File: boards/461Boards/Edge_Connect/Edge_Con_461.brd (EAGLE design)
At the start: 56.8 x 57.1 mm, 8 parts, among them IC1 TINY26P

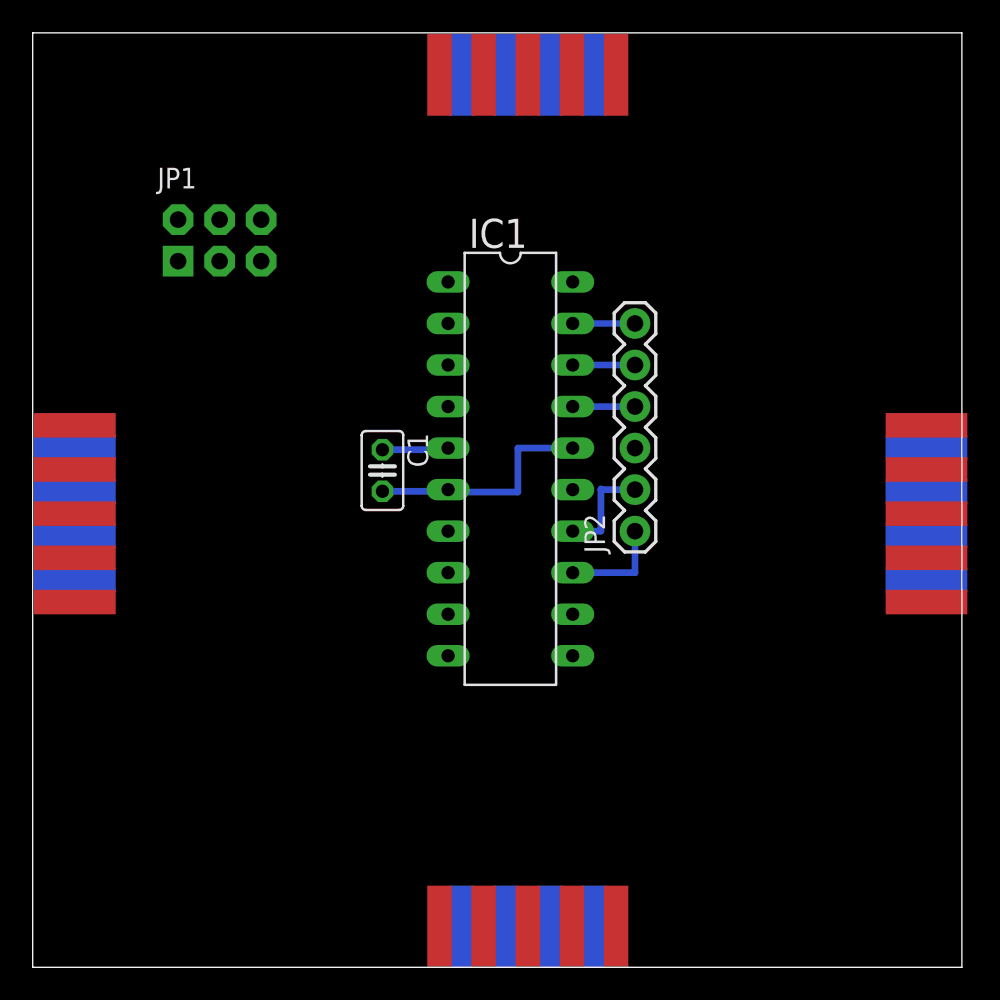
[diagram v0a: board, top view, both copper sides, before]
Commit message: Layout in progress, one footprint needs to be added to 461_Edge Connect prior to cut.
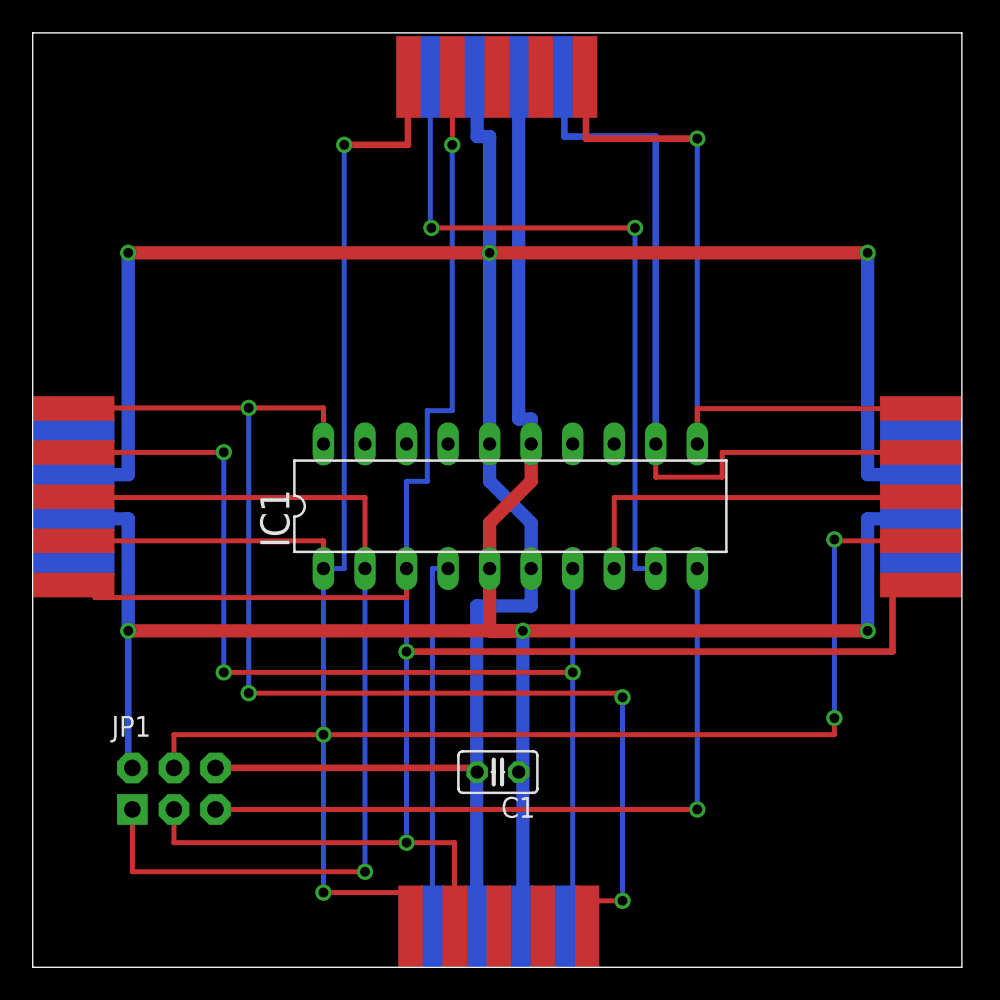
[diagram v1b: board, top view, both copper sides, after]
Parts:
- removed JP2: (no value), SparkFun-Connectors:1X06
- moved JP1 33.6 mm to (8.64, 10.9)
- moved C1 19.7 mm to (28.4, 11.9), turned to 180 degrees
- moved RIGHT 14.4 mm to (51.8, 34.9), turned to 270 degrees
- moved LEFT 14.3 mm to (0.00, 34.9), turned to 270 degrees
- moved IC1 2.29 mm to (29.2, 28.2), turned to 0 degrees
- moved UP 1.91 mm to (22.2, 51.9)
- moved DOWN 1.78 mm to (22.4, 0.00)
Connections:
- removed net 16: JP2.3
- net 13: no longer JP2.1
- net 14: no longer JP2.2
- net 17: no longer JP2.4
- net 18: no longer JP2.5
- net 19: no longer JP2.6
- net CLK_IN: now also DOWN.P$9, LEFT.P$2; no longer DOWN.P$1, LEFT.P$1
- net CLK_OUT: now also RIGHT.P$2, UP.P$9; no longer RIGHT.P$1, UP.P$1
- net DOWN: now also DOWN.P$6; no longer DOWN.P$2
- net GND: no longer DOWN.P$8, LEFT.P$8, RIGHT.P$8, UP.P$8
- net LEFT: now also LEFT.P$3; no longer LEFT.P$2
- net MDO: now also RIGHT.P$1; no longer RIGHT.P$5
- net RIGHT: now also RIGHT.P$3; no longer RIGHT.P$2
- net SCL: now also DOWN.P$2, LEFT.P$5, RIGHT.P$5, UP.P$2; no longer DOWN.P$4, LEFT.P$4, RIGHT.P$4, UP.P$4
- net SDA: now also DOWN.P$1, LEFT.P$4, RIGHT.P$4, UP.P$1; no longer DOWN.P$3, LEFT.P$3, RIGHT.P$3, UP.P$3
- net SDI: now also LEFT.P$1; no longer LEFT.P$5
- net UP: now also UP.P$6; no longer UP.P$2
- net VCC: now also DOWN.P$8, LEFT.P$8, RIGHT.P$8, UP.P$8; no longer DOWN.P$6, DOWN.P$9, LEFT.P$6, LEFT.P$9, RIGHT.P$6, RIGHT.P$9, UP.P$6, UP.P$9
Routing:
- net SDA: track 0.00 -> 139.1 mm, vias 0 -> 5
- net GND: track 14.5 -> 152.5 mm, vias 0 -> 3
- net SCL: track 0.00 -> 132.4 mm, vias 0 -> 3
- net VCC: track 5.13 -> 130.3 mm, vias 0 -> 3
- net SDI: track 0.00 -> 71.3 mm, vias 0 -> 4
- net CLK_IN: track 0.00 -> 64.2 mm, vias 0 -> 3
- net LEFT: track 0.00 -> 57.3 mm, vias 0 -> 1
- net CLK_OUT: track 0.00 -> 50.1 mm
- net MDO: track 0.00 -> 49.3 mm, vias 0 -> 1
- net UP: track 0.00 -> 44.7 mm, vias 0 -> 2
- net N$1: track 0.00 -> 44.2 mm, vias 0 -> 1
- net RIGHT: track 0.00 -> 24.5 mm
- net DOWN: track 0.00 -> 22.0 mm
- net 14: track 6.40 -> 0.00 mm
- net 13: track 6.35 -> 0.00 mm
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
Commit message: Edge Connect Layout Complete V1.0, 3 Jumper Function Select, 2 LED spaces available, Push Button Reset.
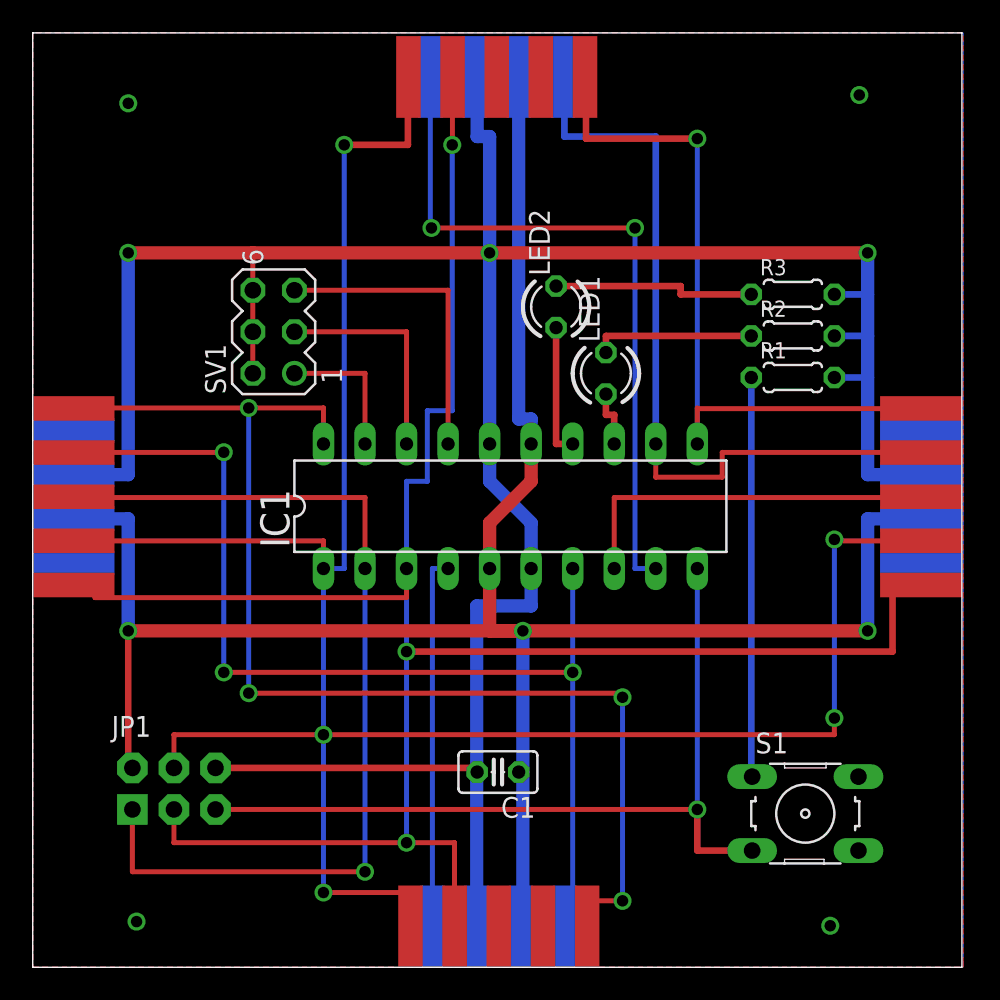
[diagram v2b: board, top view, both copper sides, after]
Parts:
- added LED1, LED2: (no value), led:LED3MM
- added R1, R2, R3: (no value), rcl:0204/5
- added S1: (no value), switch-omron:B3F-10XX
- added SV1: (no value), con-lstb:MA03-2
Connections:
- new net N$2: R1.1, S1.1
- new net N$3: LED1.K, R2.1
- new net N$4: LED2.K, R3.1
- net 13: now also LED1.A
- net 14: now also LED2.A
- net 17: now also SV1.5
- net 18: now also SV1.3
- net 19: now also SV1.1
- net GND: now also R1.2, R2.2, R3.2, SV1.2, SV1.4, SV1.6
- net N$1: now also S1.3
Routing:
- net N$2: track 0.00 -> 24.5 mm
- net 17: track 0.00 -> 18.8 mm
- net 18: track 0.00 -> 13.7 mm
- net GND: track 152.5 -> 165.9 mm, vias 3 -> 7
- net N$4: track 0.00 -> 12.4 mm
- net N$3: track 0.00 -> 9.91 mm
- net 19: track 0.00 -> 8.64 mm
- net 14: track 0.00 -> 8.13 mm
- net N$1: track 44.2 -> 50.1 mm
- net 13: track 0.00 -> 3.56 mm
- added copper zone on layer 1, net GND
- added copper zone on layer 16, net GND

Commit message: Moved Pull-up resistor to be pull up resistor on Edge Connect 461 board.
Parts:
- moved R1 9.52 mm to (45.0, 26.7), turned to 270 degrees
- moved S1 2.55 mm to (49.8, 9.65)
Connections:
- removed net N$2: R1.1, S1.1
- net GND: now also S1.1; no longer R1.2
- net N$1: now also R1.2
- net VCC: now also R1.1
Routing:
- net N$2: track 24.5 -> 0.00 mm
- net GND: track 165.9 -> 183.3 mm
- net VCC: track 130.6 -> 138.5 mm
- net N$1: track 50.1 -> 57.3 mm
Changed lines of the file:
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@@
 <attribute name="OC_FARNELL" value="unknown" x="14.732" y="38.862" size="1.778" layer="27" rot="R90" display="off"/>
 </element>
-<element name="S1" library="switch-omron" package="B3F-10XX" value="" x="47.244" y="9.398">
-<attribute name="OC_NEWARK" value="36M3542" x="47.244" y="9.398" size="1.778" layer="27" display="off"/>
-<attribute name="MPN" value="B3F-1000" x="47.244" y="9.398" size="1.778" layer="27" display="off"/>
-<attribute name="MF" value="" x="47.244" y="9.398" size="1.778" layer="27" display="off"/>
-<attribute name="OC_FARNELL" value="176432" x="47.244" y="9.398" size="1.778" layer="27" display="off"/>
+<element name="S1" library="switch-omron" package="B3F-10XX" value="" x="49.784" y="9.652">
+<attribute name="OC_NEWARK" value="36M3542" x="49.784" y="9.652" size="1.778" layer="27" display="off"/>
+<attribute name="MPN" value="B3F-1000" x="49.784" y="9.652" size="1.778" layer="27" display="off"/>
+<attribute name="MF" value="" x="49.784" y="9.652" size="1.778" layer="27" display="off"/>
+<attribute name="OC_FARNELL" value="176432" x="49.784" y="9.652" size="1.778" layer="27" display="off"/>
 </element>
-<element name="R1" library="rcl" package="0204/5" value="" x="46.482" y="36.068"/>
+<element name="R1" library="rcl" package="0204/5" value="" x="44.958" y="26.67" rot="R270"/>
 <element name="R2" library="rcl" package="0204/5" value="" x="46.482" y="38.608"/>
 <element name="R3" library="rcl" package="0204/5" value="" x="46.482" y="41.148"/>
@@
 <wire x1="5.842" y1="20.574" x2="5.842" y2="12.192" width="0.4064" layer="1"/>
 <wire x1="5.842" y1="12.192" x2="6.096" y2="12.192" width="0.4064" layer="1"/>
+<contactref element="R1" pad="1"/>
+<wire x1="44.958" y1="29.21" x2="47.498" y2="29.21" width="0.4064" layer="16"/>
+<wire x1="47.498" y1="29.21" x2="47.498" y2="27.425" width="0.4064" layer="16"/>
+<wire x1="47.498" y1="27.425" x2="51.054" y2="27.425" width="0.4064" layer="16"/>
 </signal>
 <signal name="GND">
@@
 <wire x1="13.462" y1="43.688" x2="27.94" y2="43.688" width="0.8128" layer="1"/>
 <wire x1="55.126" y1="30.125" x2="51.054" y2="30.125" width="0.8128" layer="16"/>
-<wire x1="51.054" y1="30.125" x2="51.054" y2="36.068" width="0.8128" layer="16"/>
+<wire x1="51.054" y1="30.125" x2="51.054" y2="38.608" width="0.8128" layer="16"/>
 <via x="51.054" y="43.688" extent="1-16" drill="0.7"/>
-<wire x1="51.054" y1="36.068" x2="51.054" y2="38.608" width="0.8128" layer="16"/>
 <wire x1="51.054" y1="38.608" x2="51.054" y2="41.148" width="0.8128" layer="16"/>
 <wire x1="51.054" y1="41.148" x2="51.054" y2="43.688" width="0.8128" layer="16"/>
@@
 <wire x1="13.462" y1="38.862" x2="13.462" y2="41.402" width="0.3048" layer="1"/>
 <wire x1="13.462" y1="41.402" x2="13.462" y2="43.688" width="0.3048" layer="1"/>
-<contactref element="R1" pad="2"/>
 <contactref element="R2" pad="2"/>
 <contactref element="R3" pad="2"/>
 <wire x1="49.022" y1="41.148" x2="51.054" y2="41.148" width="0.4064" layer="16"/>
 <wire x1="49.022" y1="38.608" x2="51.054" y2="38.608" width="0.4064" layer="16"/>
-<wire x1="49.022" y1="36.068" x2="51.054" y2="36.068" width="0.4064" layer="16"/>
 <polygon width="0.4064" layer="1" isolate="0.4064">
 <vertex x="0" y="0"/>
@@
 <via x="48.768" y="2.54" extent="1-16" drill="0.7"/>
 <via x="6.35" y="2.794" extent="1-16" drill="0.7"/>
+<contactref element="S1" pad="1"/>
+<wire x1="27.178" y1="11.938" x2="46.5074" y2="11.938" width="0.4064" layer="1"/>
+<wire x1="46.5074" y1="11.938" x2="46.5328" y2="11.9126" width="0.4064" layer="1"/>
 </signal>
 <signal name="13">
@@
 <via x="40.64" y="9.652" extent="1-16" drill="0.7"/>
 <wire x1="40.64" y1="9.652" x2="40.64" y2="24.384" width="0.3048" layer="16"/>
+<wire x1="40.64" y1="9.652" x2="40.64" y2="7.1374" width="0.4064" layer="1"/>
+<contactref element="R1" pad="2"/>
 <contactref element="S1" pad="3"/>
-<wire x1="40.64" y1="9.652" x2="40.64" y2="7.1374" width="0.4064" layer="1"/>
-<wire x1="40.64" y1="7.1374" x2="43.9928" y2="7.1374" width="0.4064" layer="1"/>
-</signal>
-<signal name="N$2">
-<contactref element="S1" pad="1"/>
-<contactref element="R1" pad="1"/>
-<wire x1="43.942" y1="36.068" x2="43.942" y2="11.6586" width="0.4064" layer="16"/>
-<wire x1="43.942" y1="11.6586" x2="43.9928" y2="11.6586" width="0.4064" layer="16"/>
+<wire x1="40.64" y1="7.1374" x2="46.2788" y2="7.1374" width="0.4064" layer="1"/>
+<wire x1="46.2788" y1="7.1374" x2="46.5328" y2="7.3914" width="0.4064" layer="1"/>
+<wire x1="40.64" y1="24.384" x2="40.64" y2="24.13" width="0.4064" layer="16"/>
+<wire x1="40.64" y1="24.13" x2="44.958" y2="24.13" width="0.4064" layer="16"/>
 </signal>
 <signal name="N$3">

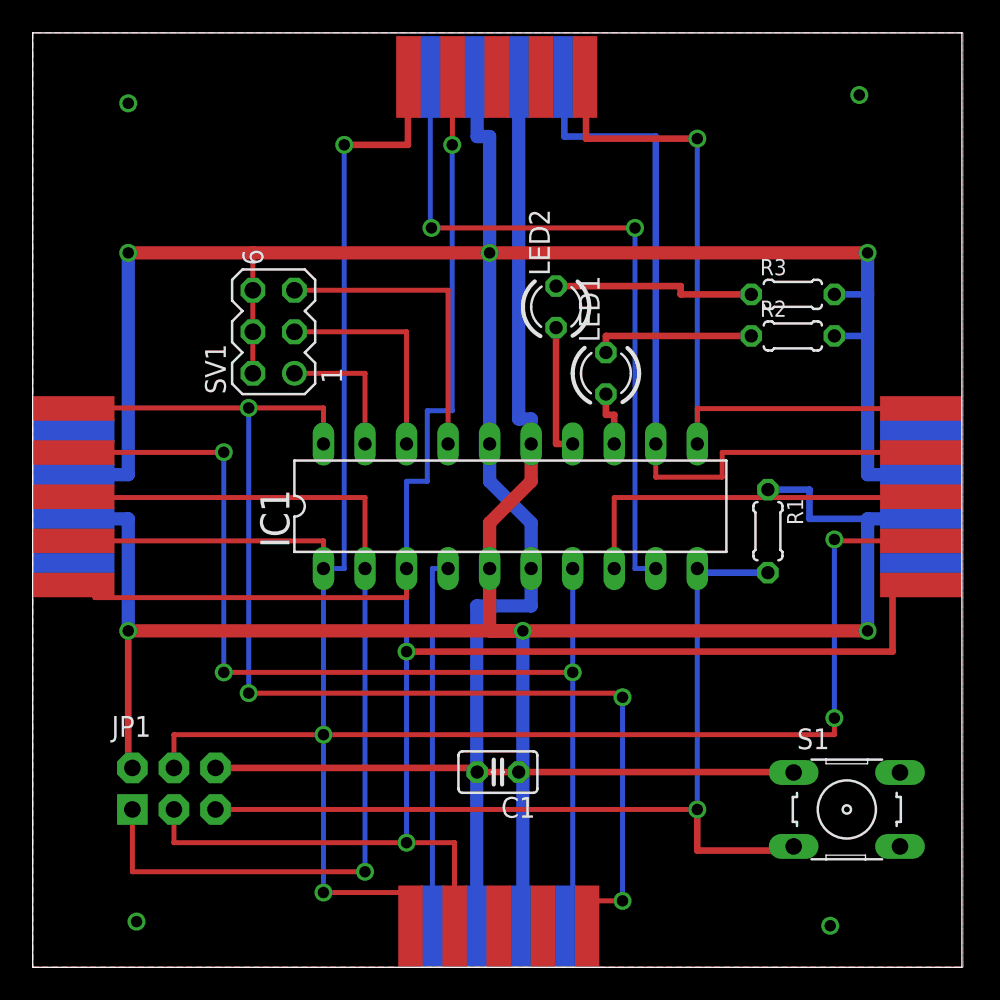
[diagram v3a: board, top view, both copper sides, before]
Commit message: v1.1 Edge Connect Prototype Board Changes: Widened power and ground traces. Added power LED indicator. Increased all via diameters for easier plating.
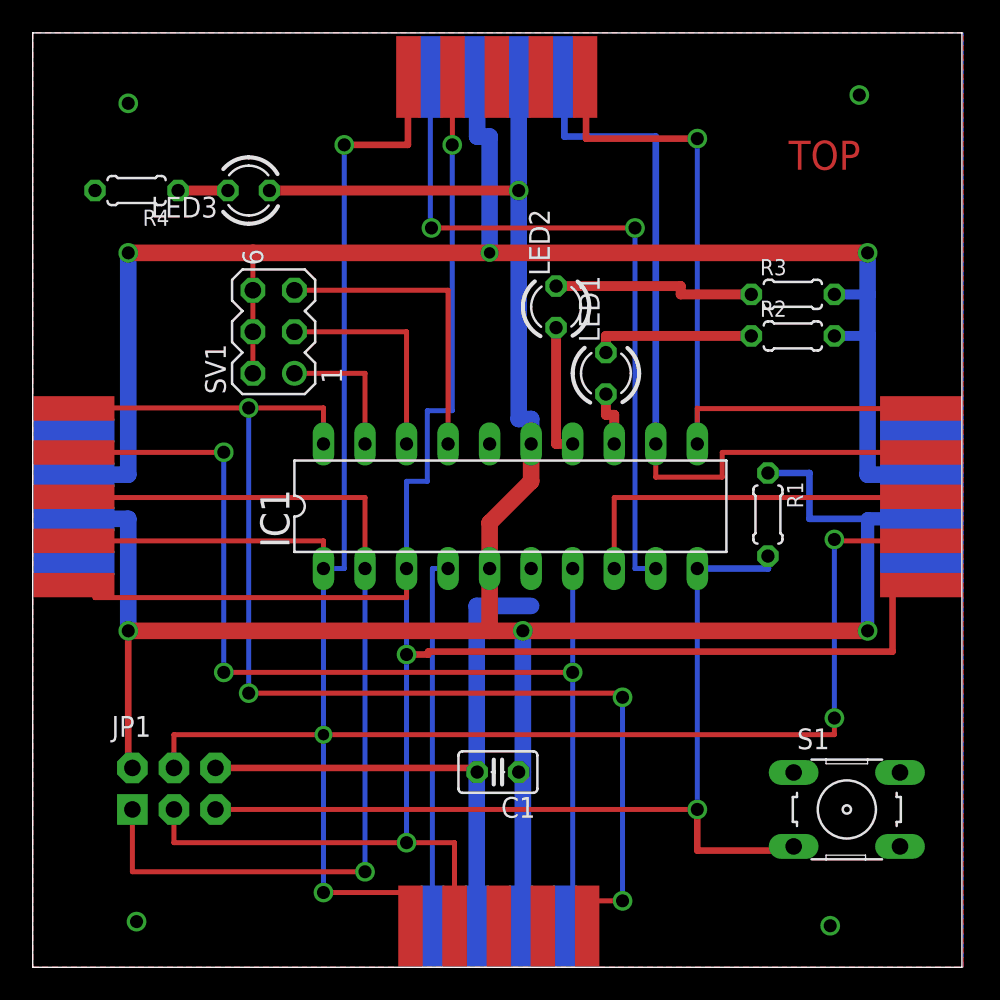
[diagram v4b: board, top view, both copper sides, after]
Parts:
- added LED3: (no value), led:LED3MM
- added R4: (no value), rcl:0204/5
- moved R1 1.02 mm to (45.0, 27.7)
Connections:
- new net N$2: LED3.K, R4.1
- net GND: now also R4.2
- net VCC: now also LED3.A
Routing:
- net GND: track 183.3 -> 141.0 mm
- net VCC: track 138.5 -> 154.7 mm, vias 3 -> 4
- net N$2: track 0.00 -> 3.05 mm
- net N$1: track 57.3 -> 57.8 mm
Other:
- board text added: "TOP"
